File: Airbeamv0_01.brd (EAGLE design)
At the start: 91.4 x 74.3 mm, 92 parts

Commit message: changed bead to one in stock
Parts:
- added CONHEADER_FAN: OFF_BOARD, Airbeam:EMPTY
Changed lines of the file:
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@@
 </element>
 <element name="U_FB1" library="Airbeam" package="U_FB1" value="FERITE_BEAD" x="16" y="39" smashed="yes" rot="R90">
-<attribute name="PARTNO" value="MH2029-300Y" x="16" y="39" size="1.778" layer="27" rot="R90" display="off"/>
+<attribute name="PARTNO" value="MH2029-600Y" x="16" y="39" size="1.778" layer="27" rot="R90" display="off"/>
 <attribute name="NAME" x="15" y="37" size="0.508" layer="25" ratio="27" rot="R90"/>
 </element>
 <element name="CA_FB1" library="Airbeam" package="U_FB1" value="FERITE_BEAD" x="6.5" y="20.5" smashed="yes" rot="R180">
-<attribute name="PARTNO" value="MH2029-300Y" x="6.5" y="20.5" size="1.778" layer="27" rot="R180" display="off"/>
+<attribute name="PARTNO" value="MH2029-600Y" x="6.5" y="20.5" size="1.778" layer="27" rot="R180" display="off"/>
 <attribute name="NAME" x="7.5" y="19.5" size="0.508" layer="25" ratio="27" rot="R180"/>
 </element>
 <element name="U_FB2" library="Airbeam" package="U_FB1" value="FERITE_BEAD" x="74" y="20" smashed="yes" rot="R180">
-<attribute name="PARTNO" value="MH2029-300Y" x="74" y="20" size="1.778" layer="27" rot="R180" display="off"/>
+<attribute name="PARTNO" value="MH2029-600Y" x="74" y="20" size="1.778" layer="27" rot="R180" display="off"/>
 <attribute name="NAME" x="75" y="19" size="0.508" layer="25" ratio="27" rot="R180"/>
 </element>
@@
 <attribute name="NAME" x="29.1" y="5.2" size="0.54" layer="51" rot="R90"/>
 </element>
+<element name="CONHEADER_FAN" library="Airbeam" package="EMPTY" value="OFF_BOARD" x="-5.2" y="-4.8">
+<attribute name="PARTNO" value="02SUR-32S" x="-5.2" y="-4.8" size="0.508" layer="27" ratio="27" display="off"/>
+</element>
 </elements>

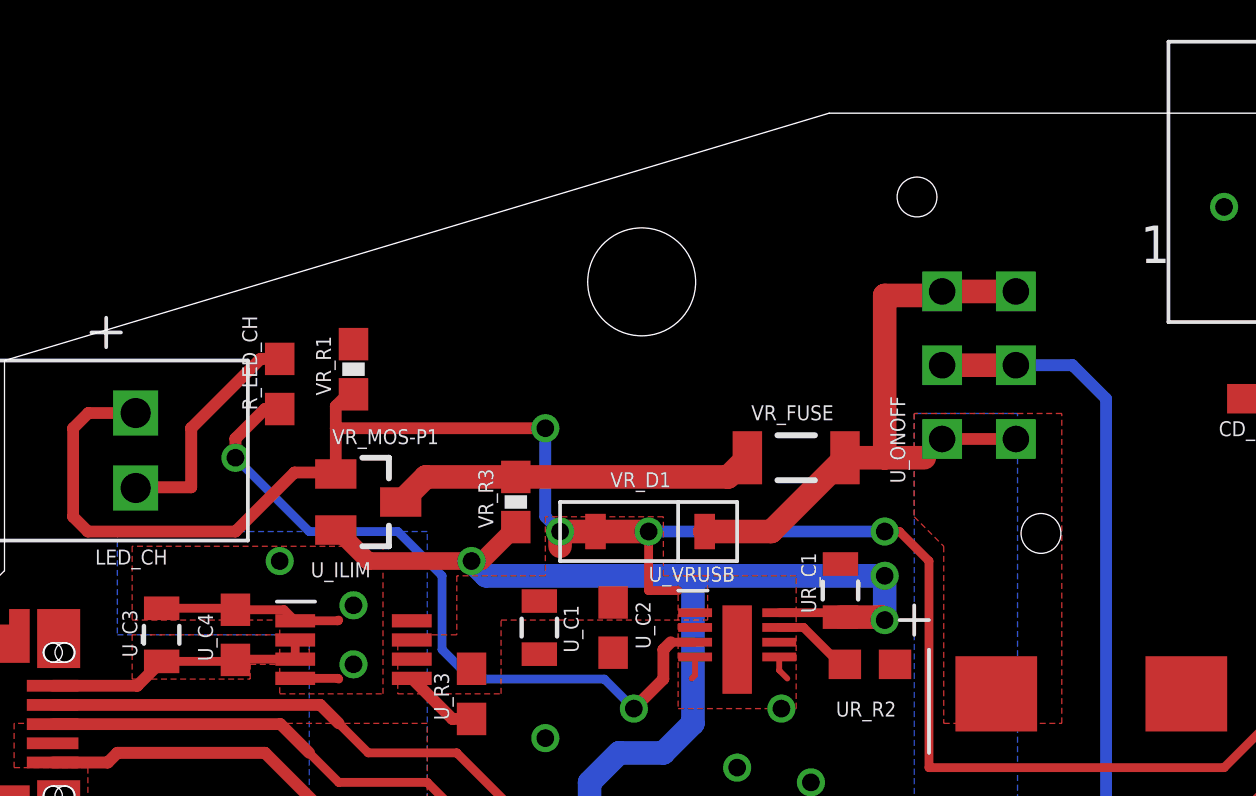
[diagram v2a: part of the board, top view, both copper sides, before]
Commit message: Fixed Switch issue, updating voltage choosing issue
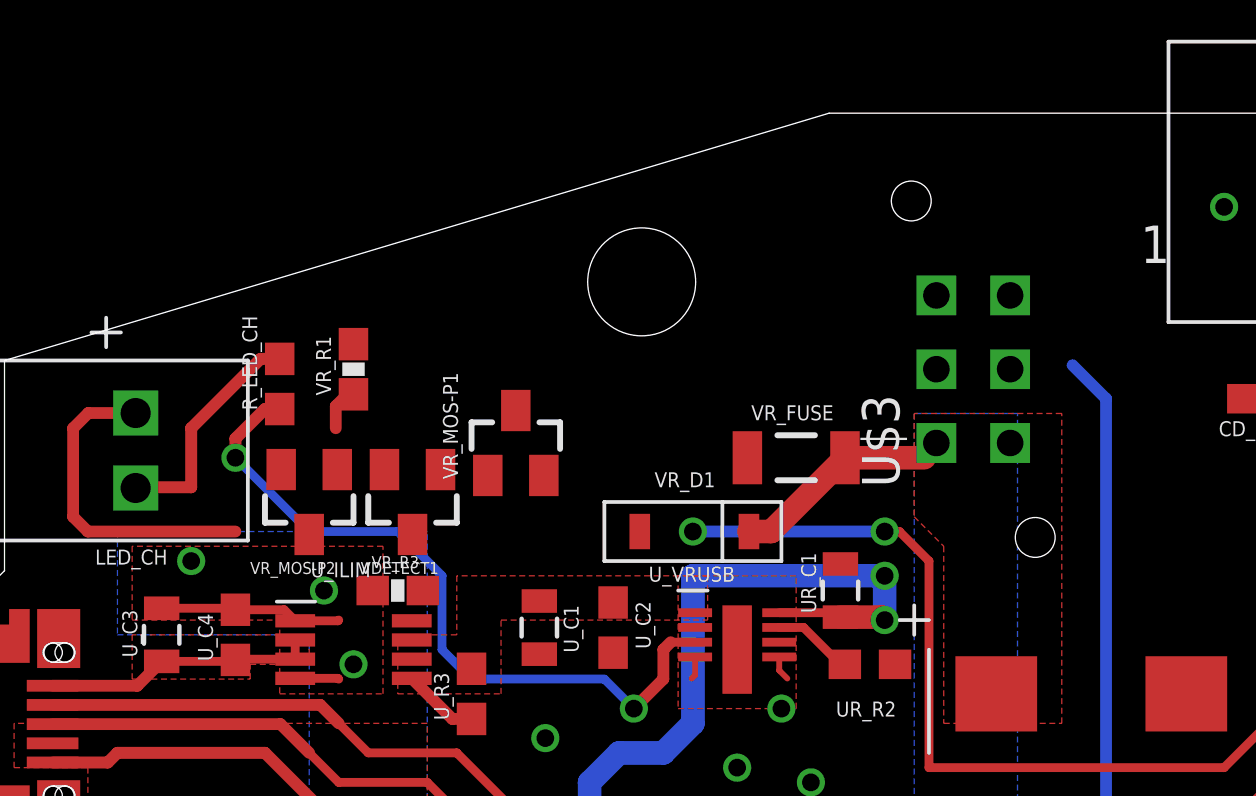
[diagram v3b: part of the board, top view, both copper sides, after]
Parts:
- removed U_ONOFF: PUSHBUTTON, Airbeam:PUSHBUTTON
- added U$3: PUSHBUTTON, Airbeam:PUSHBUTTON
- added VDETECT1: VDETEC_APX, Airbeam:SOT23
- added VR_MOS-P2: MOSFET-P, Airbeam:SOT23
- VR_R3: value DNP -> 10k
- moved VR_MOS-P1 5.39 mm to (20.5, 55.5), turned to 0 degrees
- moved VR_R3 5.00 mm to (16.5, 50.5), turned to 0 degrees
- moved VR_D1 1.50 mm to (26.5, 52.5)
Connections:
- new net N$15: VDETECT1.2, VR_MOS-P2.1
- new net VUSB_G2.9: VR_D1.P$1, VR_MOS-P1.1, VR_MOS-P2.2, VR_R1.1
- net GND: now also VDETECT1.1
- net N$5: no longer VR_R3.2
- net UGND: now also VR_R3.1
- net VDETECT_VDD: now also U$3.LS1, U$3.LS2; no longer U_ONOFF.P$2, U_ONOFF.P$5
- net VREG_IN: now also U$3.C1, U$3.C2; no longer U_ONOFF.P$1, U_ONOFF.P$3, U_ONOFF.P$4, U_ONOFF.P$6
- net VUSB: now also VDETECT1.3, VR_MOS-P2.3, VR_R3.2; no longer VR_D1.P$1, VR_MOS-P1.1, VR_R1.1
- net V_BAT: no longer VR_R3.1
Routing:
- net VUSB: track 102.5 -> 76.4 mm, vias 6 -> 4
- net V_BAT: track 49.4 -> 34.7 mm, vias 4 -> 3
- net VREG_IN: track 70.8 -> 56.8 mm
- net N$5: track 12.4 -> 0.00 mm
- net VDETECT_VDD: track 45.2 -> 40.8 mm
- net VUSB_G2.9: track 0.00 -> 1.52 mm

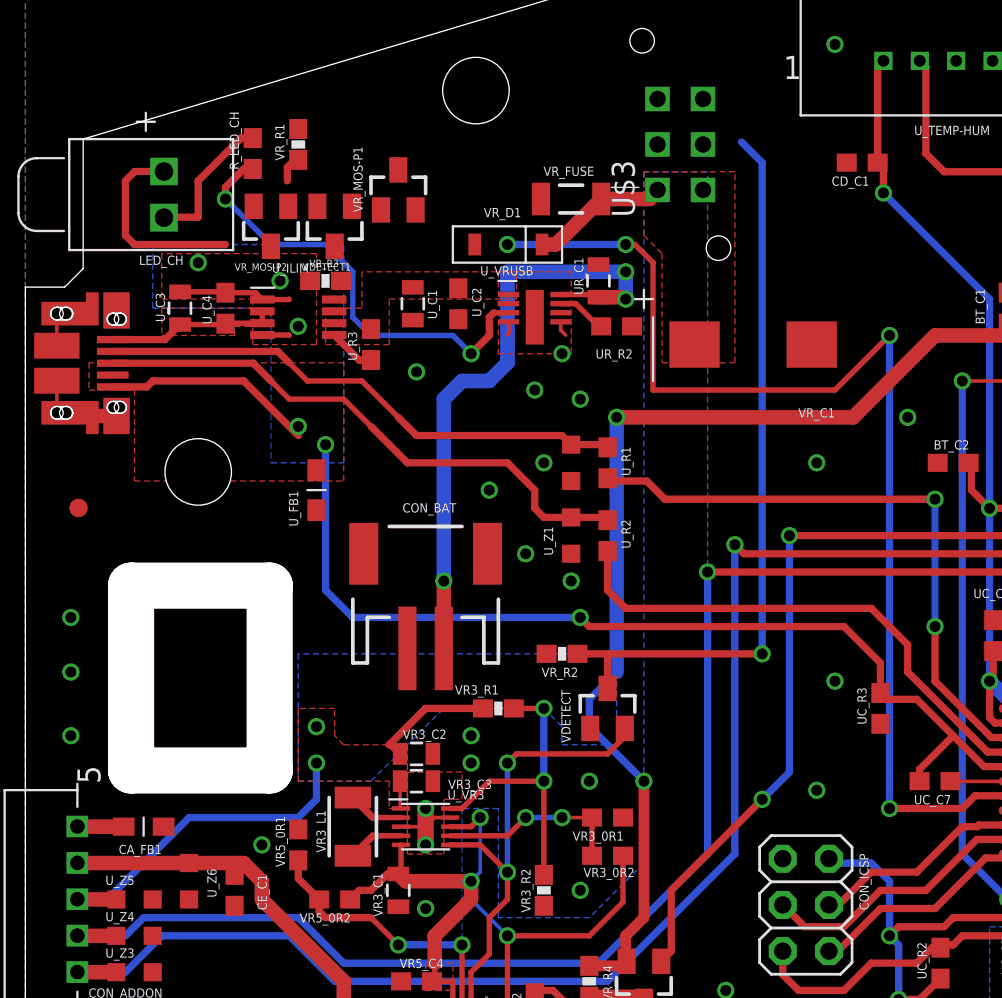
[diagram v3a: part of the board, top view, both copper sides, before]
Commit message: removed most usb + battery chips and replaced with single chip
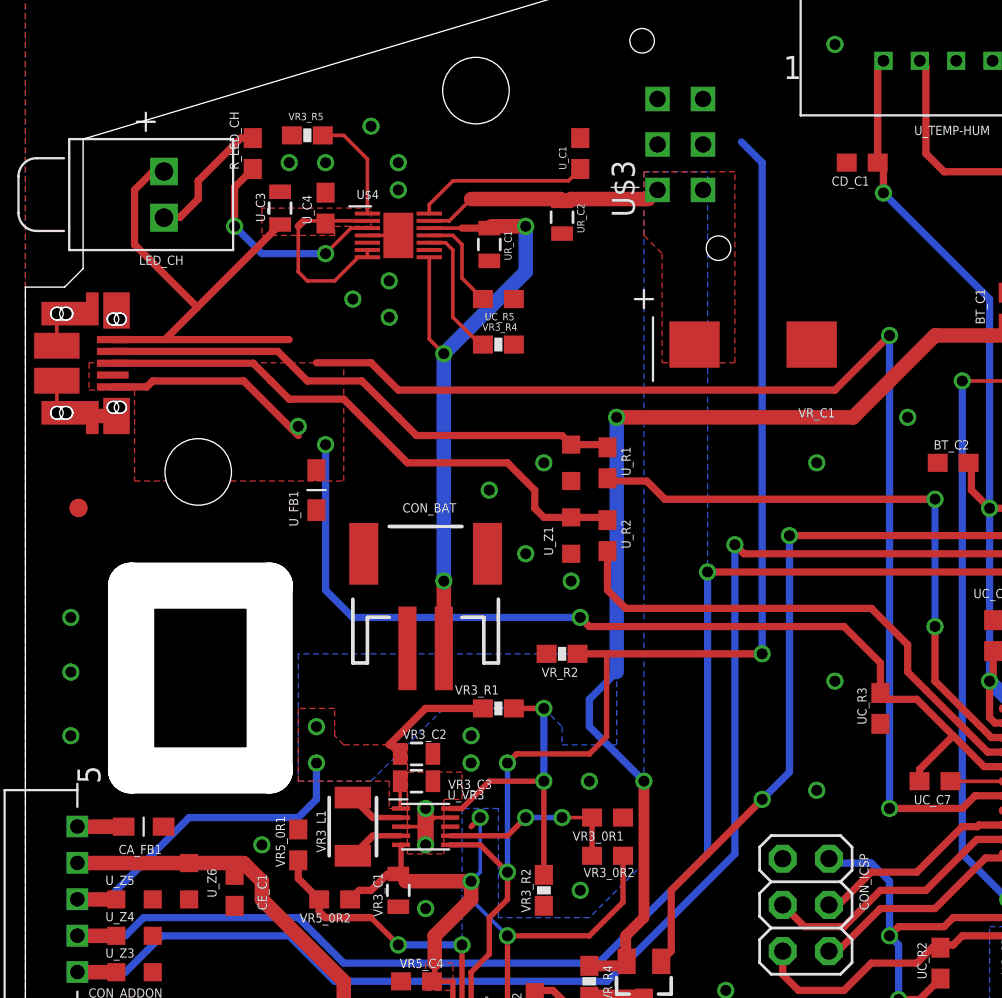
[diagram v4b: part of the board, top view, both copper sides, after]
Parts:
- removed UR_R2: 6.65k, SparkFun-Passives:0603-RES
- removed U_C2: 100nF, SparkFun-Passives:0603-CAP
- removed U_ILIM: USB-OVERCURRENT, Airbeam:MSOP-8
- removed U_R3: 10k, SparkFun-Passives:0603-RES
- removed U_VRUSB: VREG_MC34673, Airbeam:UFDFN-8
- removed VDETECT, VDETECT1: VDETEC_APX, Airbeam:SOT23
- removed VR_D1: DIODESOD123, Airbeam:SOD123_DIODE
- removed VR_FUSE: 1A, SparkFun-PowerIC:PTC-1206-WIDE
- removed VR_MOS-P1, VR_MOS-P2: MOSFET-P, Airbeam:SOT23
- removed VR_R1, VR_R3: 10k, SparkFun-Resistors:0603-RES
- added U$4: USB-BATTERY_LOAD, Airbeam:TDFN33-14
- added UC_R5: 10k, SparkFun-Passives:0603-RES
- added UR_C2: 10uF, SparkFun-Passives:0805
- added VR3_R4, VR3_R5: 86.6k, SparkFun-Resistors:0603-RES
- U_C1: value 10uF -> 100nF; device SparkFun-Passives:0805 -> SparkFun-Passives:0603-CAP
- moved CONHEADER_FAN 76.3 mm to (5.80, 70.7)
- moved U_C1 12.4 mm to (30.5, 57.5), turned to 90 degrees
- moved U_C3 7.78 mm to (14.0, 54.5)
- moved U_C4 7.78 mm to (16.5, 54.5)
- moved UR_C1 6.32 mm to (25.5, 52.5), turned to 270 degrees
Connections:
- removed net N$13: R_LED_CH.1, U_VRUSB.P$3
- removed net N$16: UR_R2.2, U_VRUSB.P$7
- removed net VDETECT_VDD: U$3.LS1, U$3.LS2, VDETECT.3, VR_R2.1
- removed net VUSB: ATMEGA32U4-T.7, LED_CH.ANODE, U_C1.1, U_C2.1, U_ILIM.P$6, U_ILIM.P$7, U_MEGA32U-Q.7, U_R3.2, U_VRUSB.P$1, VDETECT1.3, VR_MOS-P2.3, VR_R3.2
- removed net VUSB_G2.9: VR_D1.P$1, VR_MOS-P1.1, VR_MOS-P2.2, VR_R1.1
- new net N$2: U$4.P$10, VR3_R4.1
- new net N$6: U$4.P$14, U_C1.1
- net GND: now also U$4.GND_PAD, U$4.P$4, UC_R5.1, UR_C2.2, U_C3.2, U_C4.2, VR3_R4.2, VR3_R5.2; no longer UR_R2.1, U_C2.2, U_VRUSB.P$4, U_VRUSB.P$5, U_VRUSB.P$9, VDETECT.1, VDETECT1.1, VR_R1.2
- net N$15: now also U$4.P$1, VR3_R5.1; no longer VDETECT1.2, VR_MOS-P2.1
- net N$5: now also U$4.P$11, UC_R5.2; no longer VR_FUSE.1, VR_MOS-P1.3
- net N$8: now also R_LED_CH.1, U$4.P$3; no longer U_ILIM.P$5, U_R3.1
- net UGND: no longer U_C3.2, U_C4.2, U_ILIM.P$1, U_ILIM.P$4, VR_R3.1
- net VEN: now also U$3.C1, U$3.C2, VR_R2.1; no longer VDETECT.2
- net VREG_IN: now also U$3.LS1, U$3.LS2, U$4.P$13, UR_C2.1; no longer U$3.C1, U$3.C2, VR_D1.P$2, VR_FUSE.2
- net V_BAT: now also U$4.P$12, U$4.P$8; no longer U_VRUSB.P$8, VR_MOS-P1.2
- net XUSB: now also ATMEGA32U4-T.7, LED_CH.ANODE, U$4.P$2, U$4.P$6, U$4.P$7, U_MEGA32U-Q.7; no longer U_ILIM.P$2, U_ILIM.P$3
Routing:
- net XUSB: track 9.24 -> 109.1 mm, vias 0 -> 2
- net VUSB: track 76.4 -> 0.00 mm, vias 4 -> 0
- net VEN: track 27.3 -> 69.1 mm, vias 2 -> 3
- net VDETECT_VDD: track 40.8 -> 0.00 mm, vias 1 -> 0
- net N$13: track 24.6 -> 0.00 mm, vias 2 -> 0
- net N$6: track 0.00 -> 9.61 mm
- net N$8: track 2.59 -> 12.1 mm, vias 0 -> 2
- net UGND: track 75.9 -> 68.2 mm, vias 6 -> 3
- net N$2: track 0.00 -> 7.44 mm
- net N$15: track 0.00 -> 5.99 mm
- net N$5: track 0.00 -> 5.48 mm
- net N$16: track 2.74 -> 0.00 mm
- net VREG_IN: track 56.8 -> 59.2 mm
- net VUSB_G2.9: track 1.52 -> 0.00 mm
- net V_BAT: track 34.7 -> 36.0 mm
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- removed copper zone on layer 16, net UGND
- removed copper zone on layer 1, net VUSB

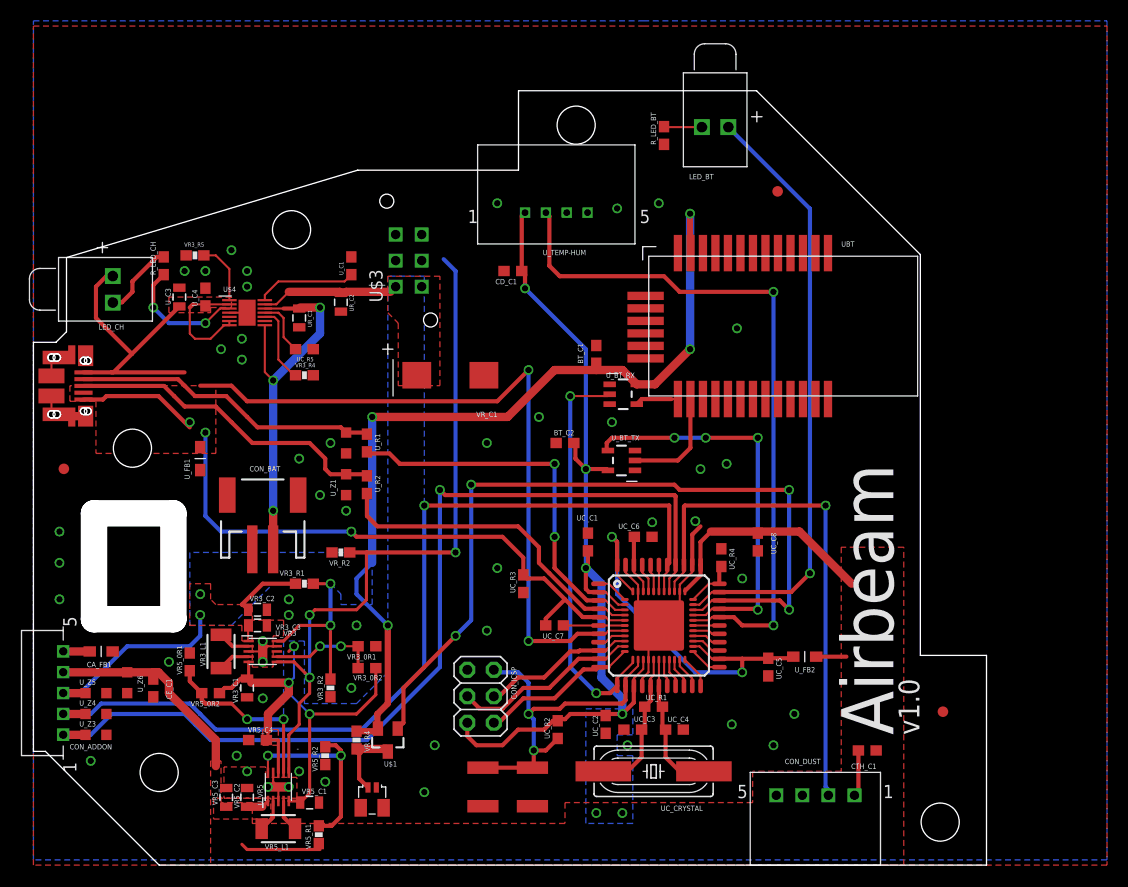
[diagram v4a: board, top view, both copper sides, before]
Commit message: updated according to Daves suggestions
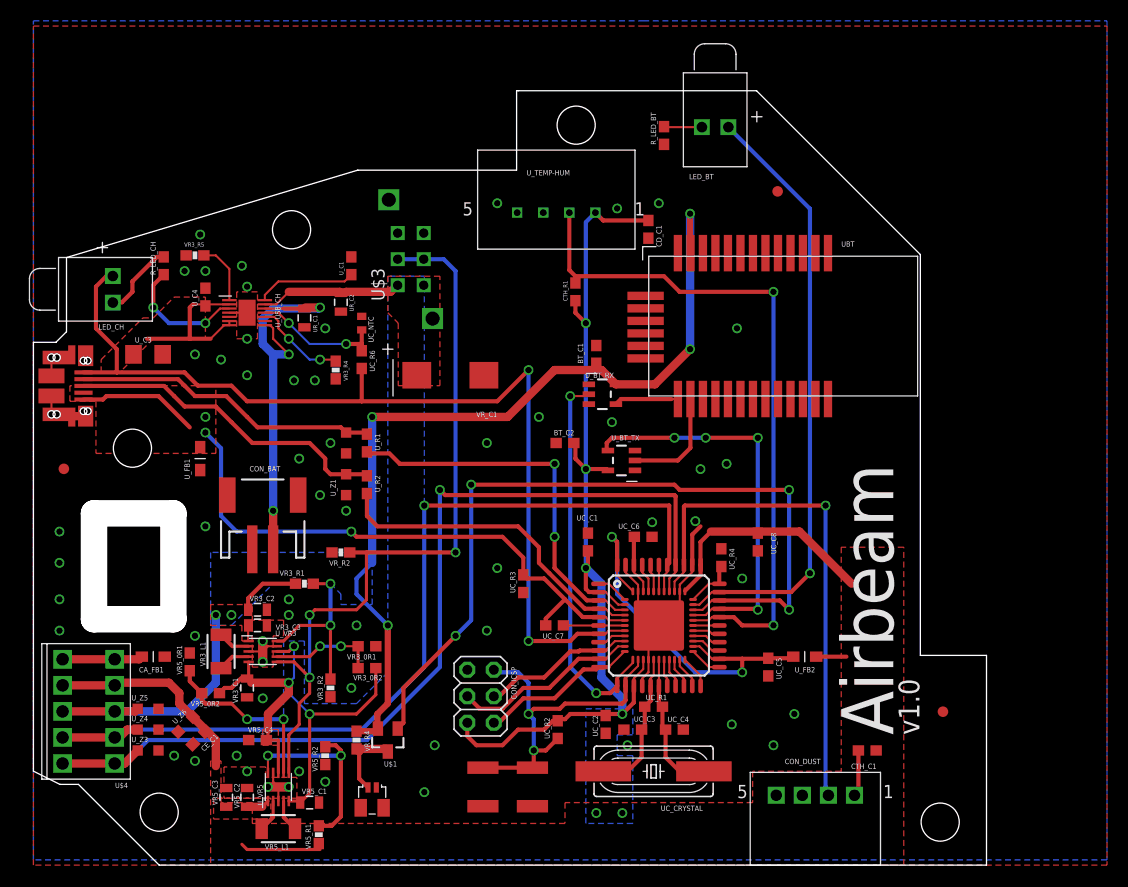
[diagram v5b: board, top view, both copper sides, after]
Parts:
- removed CON_ADDON: CON_1X52MM, Airbeam:CON_5_2MM
- removed UC_R5: 10k, SparkFun-Passives:0603-RES
- added CTH_R1, UC_R6: 10k, SparkFun-Passives:0603-RES
- added UC_NTC: 10k, Airbeam:0402
- added U_USB_CH: USB-BATTERY_LOAD, Airbeam:TDFN33-14
- U$4: value USB-BATTERY_LOAD -> TBLOCK_5; device Airbeam:TDFN33-14 -> Airbeam:TBLOCK_5
- U_C3: value 10uF -> 10uF/50V; device SparkFun-Passives:0805 -> SparkFun-Passives:1206
- moved U$4 41.2 mm to (5.30, 14.8), turned to 90 degrees
- moved CD_C1 13.6 mm to (59.0, 61.0), turned to 270 degrees
- moved U_Z6 6.88 mm to (14.6, 13.5), turned to 225 degrees
- moved CE_C1 6.51 mm to (15.9, 12.2), turned to 225 degrees
- moved U_C3 6.26 mm to (11.0, 49.0), turned to 0 degrees
- moved U_Z3 5.22 mm to (11.0, 11.0)
- moved U_Z4 5.22 mm to (11.0, 13.0)
- moved U_Z5 5.22 mm to (11.0, 15.0)
- moved CA_FB1 5.02 mm to (11.5, 20.0)
- moved CONHEADER_FAN 3.09 mm to (4.50, 73.5)
- moved VR3_R4 3.04 mm to (29.0, 47.5), turned to 270 degrees
- moved U_BT_RX 2.00 mm to (54.6, 45.2)
- moved UR_C1 0.50 mm to (26.0, 52.5)
- moved 3_3V_FAN_COPOL 0.32 mm to (4.50, 74.0)
- moved U$3 0.24 mm to (36.2, 58.1)
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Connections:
- net +3V3: now also U$4.B_3, U$4.T_3; no longer CON_ADDON.P$3
- net +5V: now also CTH_R1.1, U$4.B_4, U$4.T_4; no longer CON_ADDON.P$4
- net A1: now also U$4.B_1, U$4.T_1; no longer CON_ADDON.P$1
- net A2: now also U$4.B_2, U$4.T_2; no longer CON_ADDON.P$2
- net GND: now also UC_NTC.1, U_USB_CH.GND_PAD, U_USB_CH.P$4; no longer U$4.GND_PAD, U$4.P$4, UC_R5.1
- net IO9*/TH_DETECT: now also CTH_R1.2
- net N$15: now also U_USB_CH.P$1; no longer U$4.P$1
- net N$2: now also U_USB_CH.P$10; no longer U$4.P$10
- net N$5: now also UC_NTC.2, UC_R6.1, U_USB_CH.P$11; no longer U$4.P$11, UC_R5.2
- net N$6: now also U_USB_CH.P$14; no longer U$4.P$14
- net N$7: now also U$4.B_5, U$4.T_5; no longer CON_ADDON.P$5
- net N$8: now also U_USB_CH.P$3; no longer U$4.P$3
- net VREG_IN: now also U_USB_CH.P$13; no longer U$4.P$13
- net V_BAT: now also U_USB_CH.P$12, U_USB_CH.P$8; no longer U$4.P$12, U$4.P$8
- net XUSB: now also UC_R6.2, U_USB_CH.P$2, U_USB_CH.P$6, U_USB_CH.P$7; no longer U$4.P$2, U$4.P$6, U$4.P$7
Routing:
- net N$5: track 5.48 -> 12.5 mm, vias 0 -> 2
- net +5V: track 146.2 -> 151.6 mm
- net N$7: track 2.55 -> 7.70 mm
- net +3V3: track 114.0 -> 118.5 mm
- net VEN: track 69.1 -> 73.5 mm
- net V_BAT: track 36.0 -> 39.4 mm
- net VREG_IN: track 59.2 -> 62.5 mm
- net IO11*/BT_RX: track 38.8 -> 36.8 mm
- net BT_RX: track 4.15 -> 6.15 mm
- net XUSB: track 109.1 -> 110.8 mm
- net N$2: track 7.44 -> 8.97 mm, vias 0 -> 2
- net IO9*/TH_DETECT: track 67.9 -> 66.8 mm
- net UGND: track 68.2 -> 67.3 mm
- net A2: track 88.2 -> 87.4 mm
- net GND: vias 50 -> 57
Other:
- outline, holes or cut-outs redrawn
- board text added: "3.3V"
- board text added: "5V"
- board text added: "A1"
- board text added: "A2"
- board text added: "GND"
